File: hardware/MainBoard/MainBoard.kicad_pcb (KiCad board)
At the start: 2 copper layers, 56.9 x 28.9 mm, 25 parts, among them J1 Therm., J2 SSR, J3 Serial, J4 5Vin, J6 Keypad1, SW1 Boot Mode, SW2 RESET, U1 ESP-12F, U2 AMS1117-3.3

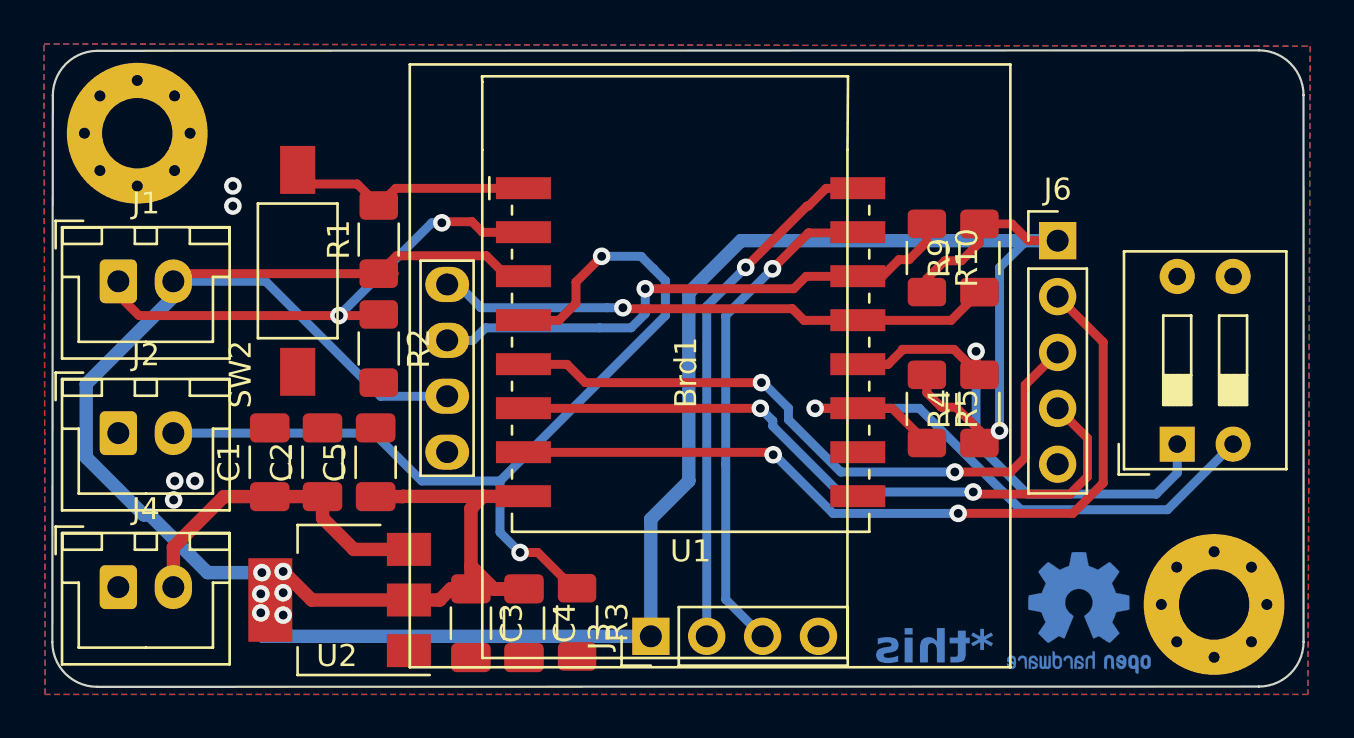
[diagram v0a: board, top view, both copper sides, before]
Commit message: fix keypad connector location on board
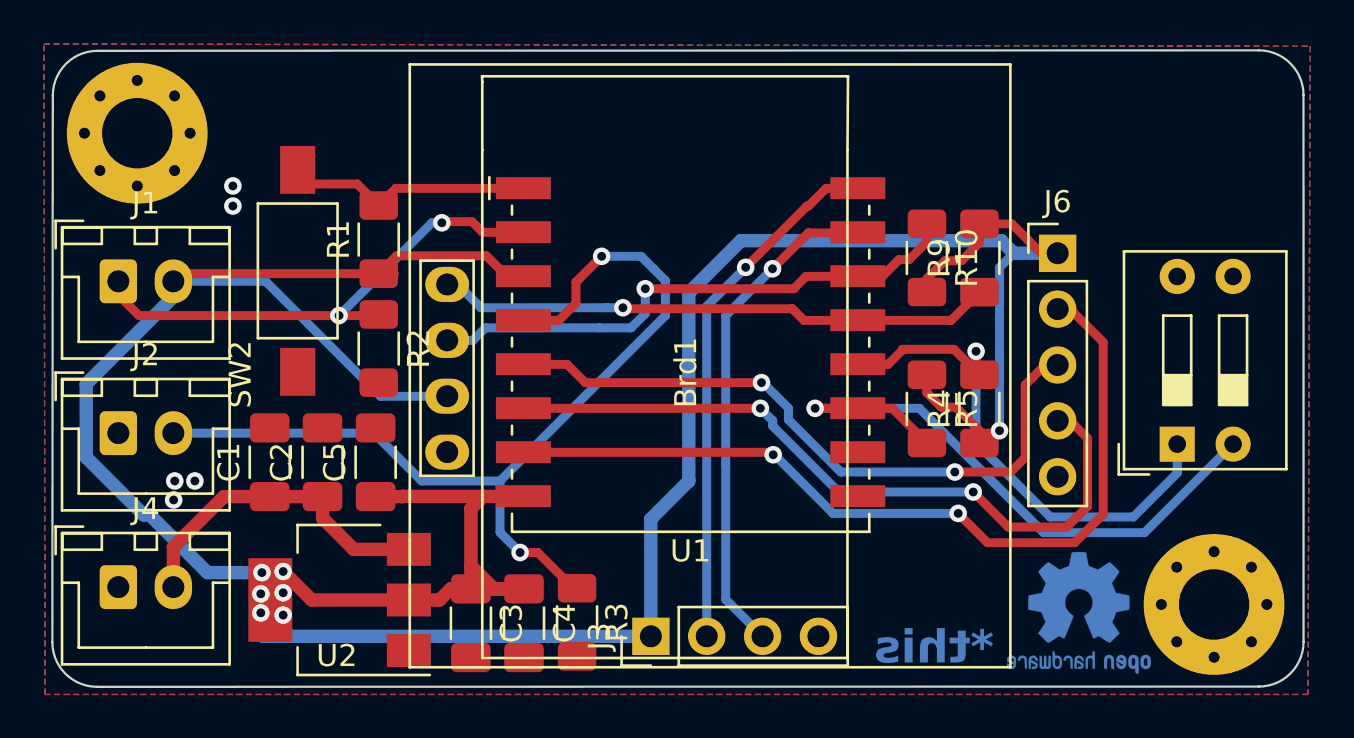
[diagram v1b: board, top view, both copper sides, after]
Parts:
- moved J6 0.57 mm to (57.7, 178.3)
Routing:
- net /IO12: track 31.4 -> 33.2 mm
- net +3V3: track 164.2 -> 162.5 mm
- net /IO13: track 37.4 -> 39.1 mm
- net /IO02: track 27.9 -> 28.7 mm
- net /IO00: track 23.4 -> 24.3 mm

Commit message: redesign pcb files
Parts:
- removed Brd1: SSD1306, SSD1306:128x64OLED
- added J5: LCD, Connector_PinHeader_2.54mm:PinHeader_1x04_P2.54mm_Vertical, F.Cu at (29.9, 187.4)
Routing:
- net +3V3: track 162.5 -> 154.3 mm
- net /IO16: track 43.6 -> 44.4 mm
